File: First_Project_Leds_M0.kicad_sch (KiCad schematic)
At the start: 0 parts

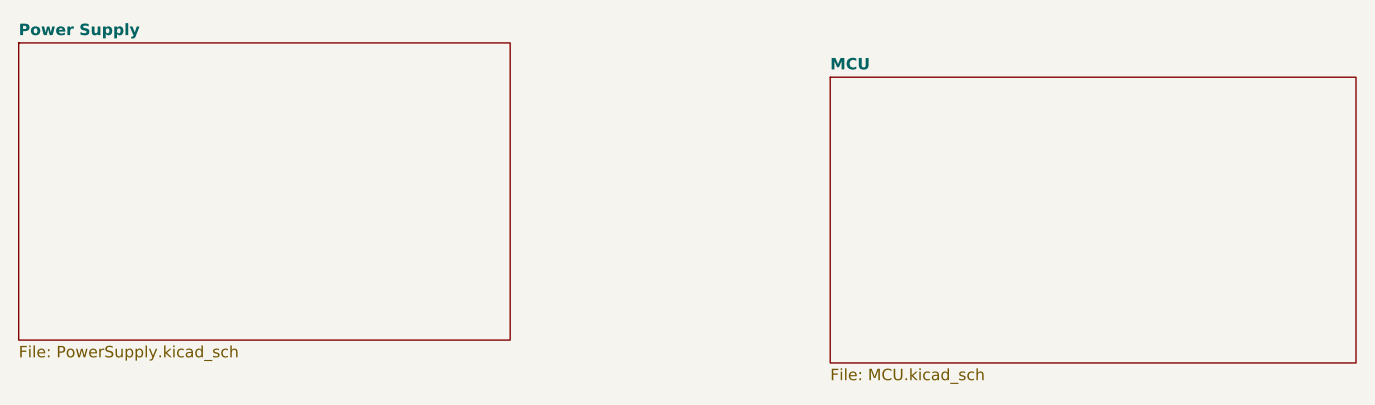
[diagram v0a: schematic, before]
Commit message: Finished Schematic design, moving on to PCB layout and routing
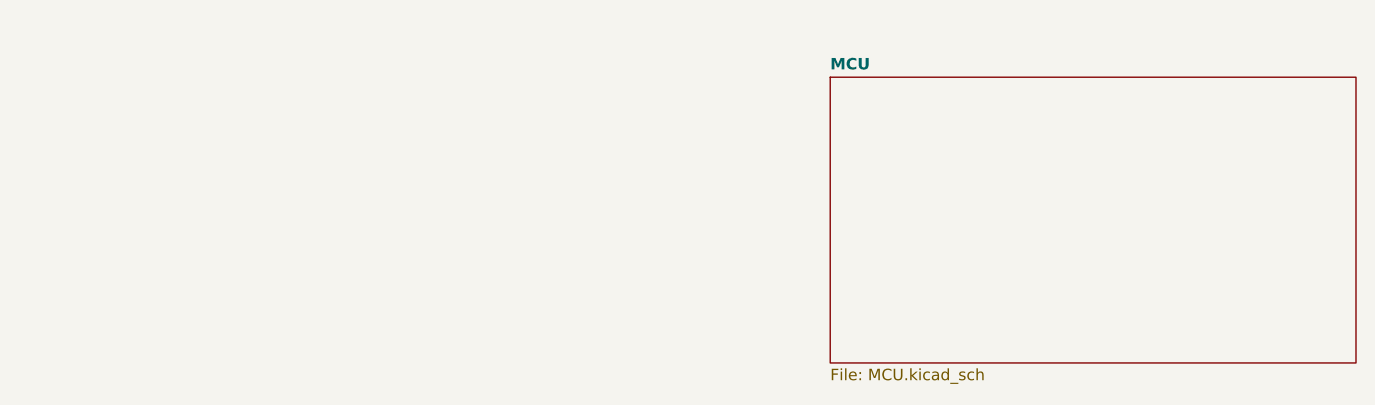
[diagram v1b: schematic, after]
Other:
- removed sheet Power Supply
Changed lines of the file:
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@@
-		)
-	)
-	(sheet
-		(at 48.26 44.45)
-		(size 54.61 33.02)
-		(fields_autoplaced yes)
-		(stroke
-			(width 0.1524)
-			(type solid)
-		)
-		(fill
-			(color 0 0 0 0.0000)
-		)
-		(property "Sheetname" "Power Supply"
-			(at 48.26 43.7384 0)
-			(show_name yes)
-			(effects
-				(font
-					(size 1.27 1.27)
-					(bold yes)
-				)
-				(justify left bottom)
-			)
-		)
-		(property "Sheetfile" "PowerSupply.kicad_sch"
-			(at 48.26 78.0546 0)
-			(effects
-				(font
-					(size 1.27 1.27)
-				)
-				(justify left top)
-			)
-		)
-		(instances
-			(project "First_Project_Leds_M0"
-				(path "/a6b7db5d-4112-4c01-9772-3f374ef07d77"
-					(page "2")
-				)
-			)
 		)
 	)
